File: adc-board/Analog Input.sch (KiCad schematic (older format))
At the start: 56 parts, among them J1 BHR-44-HUA, U1 Opamp_Quad_Generic, U2 Opamp_Quad_Generic, U29 AP7361C-33E-13, U3 Opamp_Quad_Generic, U4 Opamp_Quad_Generic, U5 Opamp_Quad_Generic, U6 Opamp_Quad_Generic

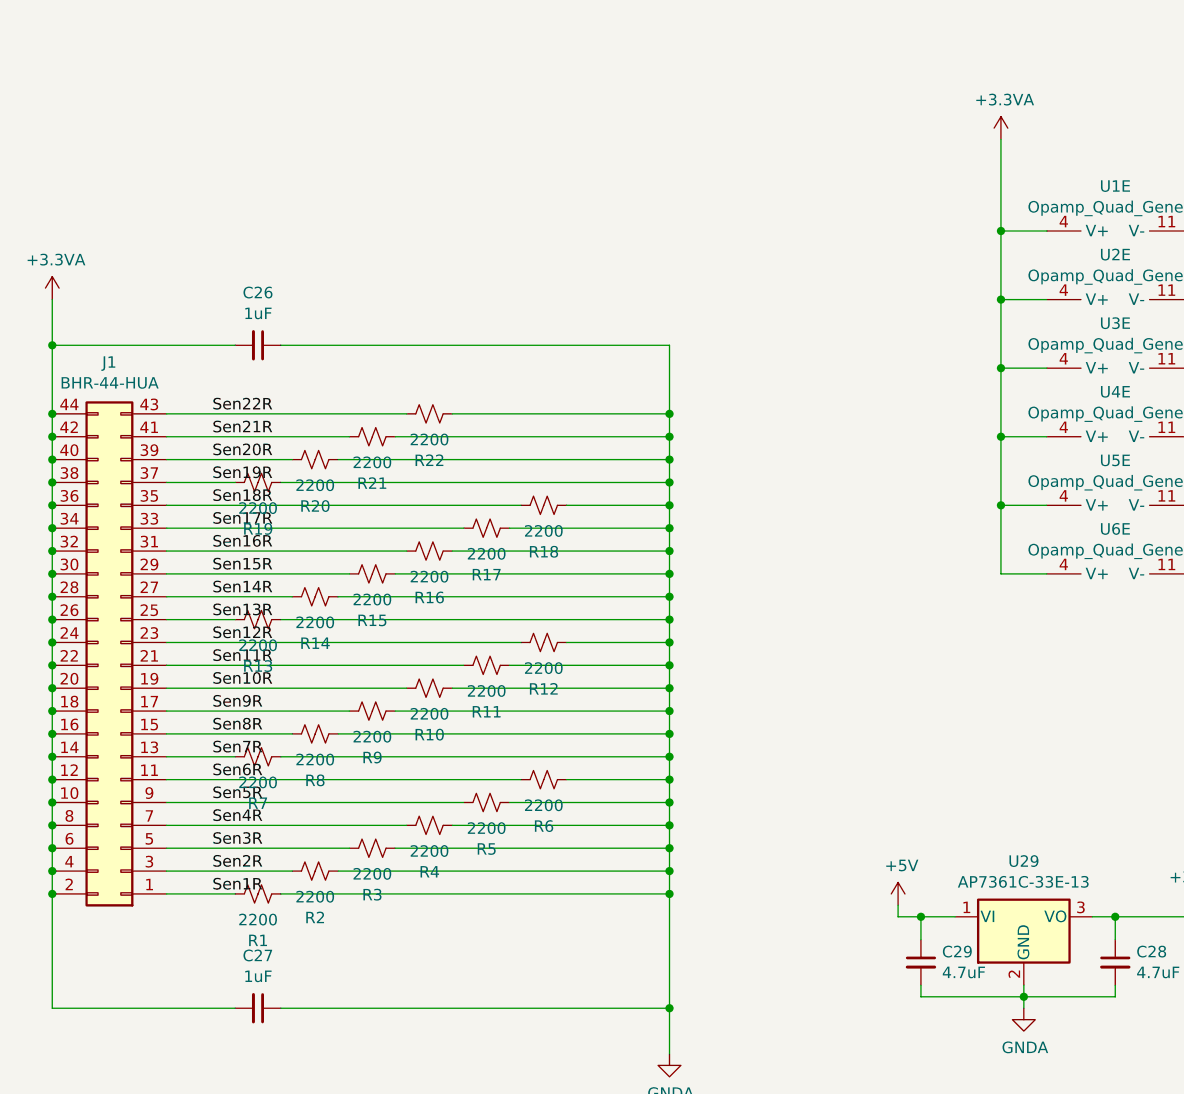
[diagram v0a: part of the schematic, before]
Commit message: correct RS485 termination resistors, adjust ground pours
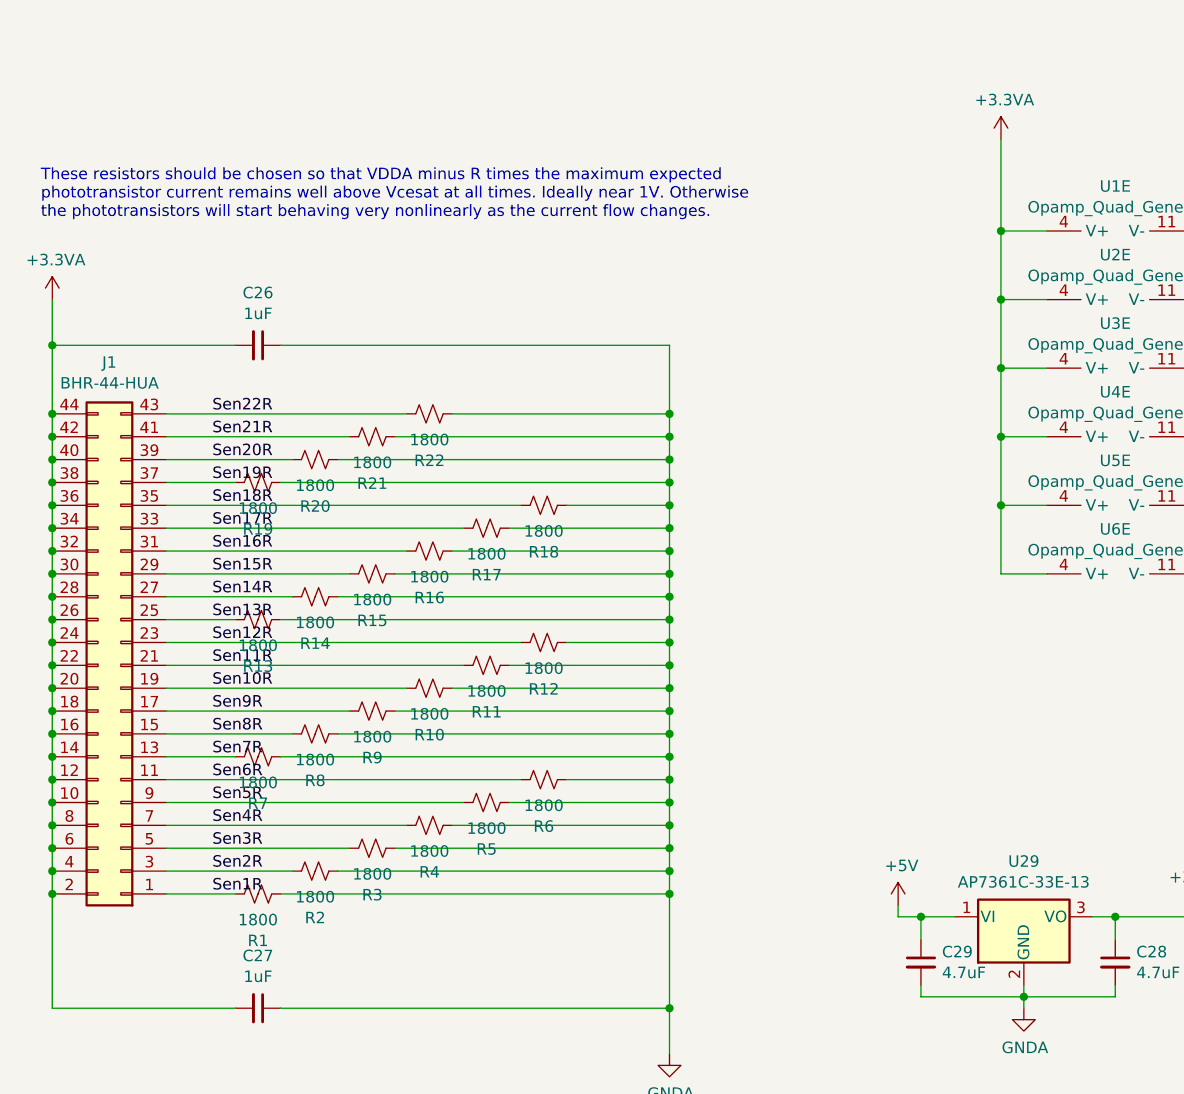
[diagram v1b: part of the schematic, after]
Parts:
- R1, R10, R11, R12, R13, R14, R15, R16, R17, R18, R19, R2, R20, R21, R22, R3, R4, R5, R6, R7, R8, R9: value 2200 -> 1800
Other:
- note added: "These resistors should be chosen so that VDDA minus R times the maximum expected\nphototransistor current remains well above Vcesat at all times. Ideally near 1V. Otherwise\nthe phototransistors will start behaving very nonlinearly as the current flow changes."
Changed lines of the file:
@@
 P 1850 6300
 F 0 "R2" V 1645 6300 50  0000 C CNN
-F 1 "2200" V 1736 6300 50  0000 C CNN
+F 1 "1800" V 1736 6300 50  0000 C CNN
 F 2 "Resistors_SMD:R_0805" H 1850 6300 50  0001 C CNN
 F 3 "~" H 1850 6300 50  0001 C CNN
@@
 P 2100 6200
 F 0 "R3" V 1895 6200 50  0000 C CNN
-F 1 "2200" V 1986 6200 50  0000 C CNN
+F 1 "1800" V 1986 6200 50  0000 C CNN
 F 2 "Resistors_SMD:R_0805" H 2100 6200 50  0001 C CNN
 F 3 "~" H 2100 6200 50  0001 C CNN
@@
 P 2350 6100
 F 0 "R4" V 2145 6100 50  0000 C CNN
-F 1 "2200" V 2236 6100 50  0000 C CNN
+F 1 "1800" V 2236 6100 50  0000 C CNN
 F 2 "Resistors_SMD:R_0805" H 2350 6100 50  0001 C CNN
 F 3 "~" H 2350 6100 50  0001 C CNN
@@
 P 2600 6000
 F 0 "R5" V 2395 6000 50  0000 C CNN
-F 1 "2200" V 2486 6000 50  0000 C CNN
+F 1 "1800" V 2486 6000 50  0000 C CNN
 F 2 "Resistors_SMD:R_0805" H 2600 6000 50  0001 C CNN
 F 3 "~" H 2600 6000 50  0001 C CNN
@@
 P 2850 5900
 F 0 "R6" V 2645 5900 50  0000 C CNN
-F 1 "2200" V 2736 5900 50  0000 C CNN
+F 1 "1800" V 2736 5900 50  0000 C CNN
 F 2 "Resistors_SMD:R_0805" H 2850 5900 50  0001 C CNN
 F 3 "~" H 2850 5900 50  0001 C CNN
@@
 P 1600 5800
 F 0 "R7" V 1395 5800 50  0000 C CNN
-F 1 "2200" V 1486 5800 50  0000 C CNN
+F 1 "1800" V 1486 5800 50  0000 C CNN
 F 2 "Resistors_SMD:R_0805" H 1600 5800 50  0001 C CNN
 F 3 "~" H 1600 5800 50  0001 C CNN
@@
 P 1850 5700
 F 0 "R8" V 1645 5700 50  0000 C CNN
-F 1 "2200" V 1736 5700 50  0000 C CNN
+F 1 "1800" V 1736 5700 50  0000 C CNN
 F 2 "Resistors_SMD:R_0805" H 1850 5700 50  0001 C CNN
 F 3 "~" H 1850 5700 50  0001 C CNN
@@
 P 2100 5600
 F 0 "R9" V 1895 5600 50  0000 C CNN
-F 1 "2200" V 1986 5600 50  0000 C CNN
+F 1 "1800" V 1986 5600 50  0000 C CNN
 F 2 "Resistors_SMD:R_0805" H 2100 5600 50  0001 C CNN
 F 3 "~" H 2100 5600 50  0001 C CNN
@@
 P 2350 5500
 F 0 "R10" V 2145 5500 50  0000 C CNN
-F 1 "2200" V 2236 5500 50  0000 C CNN
+F 1 "1800" V 2236 5500 50  0000 C CNN
 F 2 "Resistors_SMD:R_0805" H 2350 5500 50  0001 C CNN
 F 3 "~" H 2350 5500 50  0001 C CNN
@@
 P 2600 5400
 F 0 "R11" V 2395 5400 50  0000 C CNN
-F 1 "2200" V 2486 5400 50  0000 C CNN
+F 1 "1800" V 2486 5400 50  0000 C CNN
 F 2 "Resistors_SMD:R_0805" H 2600 5400 50  0001 C CNN
 F 3 "~" H 2600 5400 50  0001 C CNN
@@
 P 2850 5300
 F 0 "R12" V 2645 5300 50  0000 C CNN
-F 1 "2200" V 2736 5300 50  0000 C CNN
+F 1 "1800" V 2736 5300 50  0000 C CNN
 F 2 "Resistors_SMD:R_0805" H 2850 5300 50  0001 C CNN
 F 3 "~" H 2850 5300 50  0001 C CNN
@@
 P 1600 5200
 F 0 "R13" V 1395 5200 50  0000 C CNN
-F 1 "2200" V 1486 5200 50  0000 C CNN
+F 1 "1800" V 1486 5200 50  0000 C CNN
 F 2 "Resistors_SMD:R_0805" H 1600 5200 50  0001 C CNN
 F 3 "~" H 1600 5200 50  0001 C CNN
@@
 P 1850 5100
 F 0 "R14" V 1645 5100 50  0000 C CNN
-F 1 "2200" V 1736 5100 50  0000 C CNN
+F 1 "1800" V 1736 5100 50  0000 C CNN
 F 2 "Resistors_SMD:R_0805" H 1850 5100 50  0001 C CNN
 F 3 "~" H 1850 5100 50  0001 C CNN
@@
 P 2100 5000
 F 0 "R15" V 1895 5000 50  0000 C CNN
-F 1 "2200" V 1986 5000 50  0000 C CNN
+F 1 "1800" V 1986 5000 50  0000 C CNN
 F 2 "Resistors_SMD:R_0805" H 2100 5000 50  0001 C CNN
 F 3 "~" H 2100 5000 50  0001 C CNN
@@
 P 2350 4900
 F 0 "R16" V 2145 4900 50  0000 C CNN
-F 1 "2200" V 2236 4900 50  0000 C CNN
+F 1 "1800" V 2236 4900 50  0000 C CNN
 F 2 "Resistors_SMD:R_0805" H 2350 4900 50  0001 C CNN
 F 3 "~" H 2350 4900 50  0001 C CNN
@@
 P 2600 4800
 F 0 "R17" V 2395 4800 50  0000 C CNN
-F 1 "2200" V 2486 4800 50  0000 C CNN
+F 1 "1800" V 2486 4800 50  0000 C CNN
 F 2 "Resistors_SMD:R_0805" H 2600 4800 50  0001 C CNN
 F 3 "~" H 2600 4800 50  0001 C CNN
@@
 P 2850 4700
 F 0 "R18" V 2645 4700 50  0000 C CNN
-F 1 "2200" V 2736 4700 50  0000 C CNN
+F 1 "1800" V 2736 4700 50  0000 C CNN
 F 2 "Resistors_SMD:R_0805" H 2850 4700 50  0001 C CNN
 F 3 "~" H 2850 4700 50  0001 C CNN
@@
 P 1600 4600
 F 0 "R19" V 1395 4600 50  0000 C CNN
-F 1 "2200" V 1486 4600 50  0000 C CNN
+F 1 "1800" V 1486 4600 50  0000 C CNN
 F 2 "Resistors_SMD:R_0805" H 1600 4600 50  0001 C CNN
 F 3 "~" H 1600 4600 50  0001 C CNN
@@
 P 1850 4500
 F 0 "R20" V 1645 4500 50  0000 C CNN
-F 1 "2200" V 1736 4500 50  0000 C CNN
+F 1 "1800" V 1736 4500 50  0000 C CNN
 F 2 "Resistors_SMD:R_0805" H 1850 4500 50  0001 C CNN
 F 3 "~" H 1850 4500 50  0001 C CNN
@@
 P 2100 4400
 F 0 "R21" V 1895 4400 50  0000 C CNN
-F 1 "2200" V 1986 4400 50  0000 C CNN
+F 1 "1800" V 1986 4400 50  0000 C CNN
 F 2 "Resistors_SMD:R_0805" H 2100 4400 50  0001 C CNN
 F 3 "~" H 2100 4400 50  0001 C CNN
@@
 P 2350 4300
 F 0 "R22" V 2145 4300 50  0000 C CNN
-F 1 "2200" V 2236 4300 50  0000 C CNN
+F 1 "1800" V 2236 4300 50  0000 C CNN
 F 2 "Resistors_SMD:R_0805" H 2350 4300 50  0001 C CNN
 F 3 "~" H 2350 4300 50  0001 C CNN
@@
 P 1600 6400
 F 0 "R1" V 1395 6400 50  0000 C CNN
-F 1 "2200" V 1486 6400 50  0000 C CNN
+F 1 "1800" V 1486 6400 50  0000 C CNN
 F 2 "Resistors_SMD:R_0805" H 1600 6400 50  0001 C CNN
 F 3 "~" H 1600 6400 50  0001 C CNN
@@
 Wire Wire Line
 	5350 6500 5700 6500
+Text Notes 650  3450 0    50   ~ 0
+These resistors should be chosen so that VDDA minus R times the maximum expected\nphototransistor current remains well above Vcesat at all times. Ideally near 1V. Otherwise\nthe phototransistors will start behaving very nonlinearly as the current flow changes.
 $EndSCHEMATC

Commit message: alternative power inputs; cap on NRST; 3.3V reg thermal work on PCB
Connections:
- net +3.3VA: now also U6.10 (+), U6.12 (+)
- net GNDA: no longer U6.10 (+), U6.12 (+)
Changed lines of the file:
@@
 	12800 7800 12850 7800
 Wire Wire Line
-	10800 7800 10800 7600
-Wire Wire Line
 	10800 7600 10850 7600
-Wire Wire Line
-	12800 7800 12800 7600
 Wire Wire Line
 	12800 7600 12850 7600
@@
 Wire Wire Line
 	12800 7800 12800 7900
-Connection ~ 12800 7800
 Wire Wire Line
 	10800 7800 10800 7900
-Connection ~ 10800 7800
 $Comp
 L Device:Opamp_Quad_Generic U1
@@
 Text Notes 650  3450 0    50   ~ 0
 These resistors should be chosen so that VDDA minus R times the maximum expected\nphototransistor current remains well above Vcesat at all times. Ideally near 1V. Otherwise\nthe phototransistors will start behaving very nonlinearly as the current flow changes.
+$Comp
+L power:+3.3VA #PWR0137
+U 1 1 5FB624A5
+P 10800 7550
+F 0 "#PWR0137" H 10800 7400 50  0001 C CNN
+F 1 "+3.3VA" H 10815 7723 50  0000 C CNN
+F 2 "" H 10800 7550 50  0001 C CNN
+F 3 "" H 10800 7550 50  0001 C CNN
+	1    10800 7550
+	1    0    0    -1
+$EndComp
+$Comp
+L power:+3.3VA #PWR0140
+U 1 1 5FB64A1B
+P 12800 7550
+F 0 "#PWR0140" H 12800 7400 50  0001 C CNN
+F 1 "+3.3VA" H 12815 7723 50  0000 C CNN
+F 2 "" H 12800 7550 50  0001 C CNN
+F 3 "" H 12800 7550 50  0001 C CNN
+	1    12800 7550
+	1    0    0    -1
+$EndComp
+Wire Wire Line
+	12800 7600 12800 7550
+Wire Wire Line
+	10800 7600 10800 7550
 $EndSCHEMATC

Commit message: move USB ferrite closer to connector; add VCC pad near BOOT pulldown
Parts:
- U29: value AP7361C-33E-13 -> AP2114HA-3.3TRG1
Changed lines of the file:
@@
 AR Path="/5FA7E425/60593179" Ref="U29"  Part="1"
 F 0 "U29" H 4950 6742 50  0000 C CNN
-F 1 "AP7361C-33E-13" H 4950 6651 50  0000 C CNN
+F 1 "AP2114HA-3.3TRG1" H 4950 6651 50  0000 C CNN
 F 2 "TO_SOT_Packages_SMD:SOT-223-3_TabPin2" H 4950 6725 50  0001 C CIN
 F 3 "https://www.diodes.com/assets/Datasheets/AP7361C.pdf" H 4950 6450 50  0001 C CNN

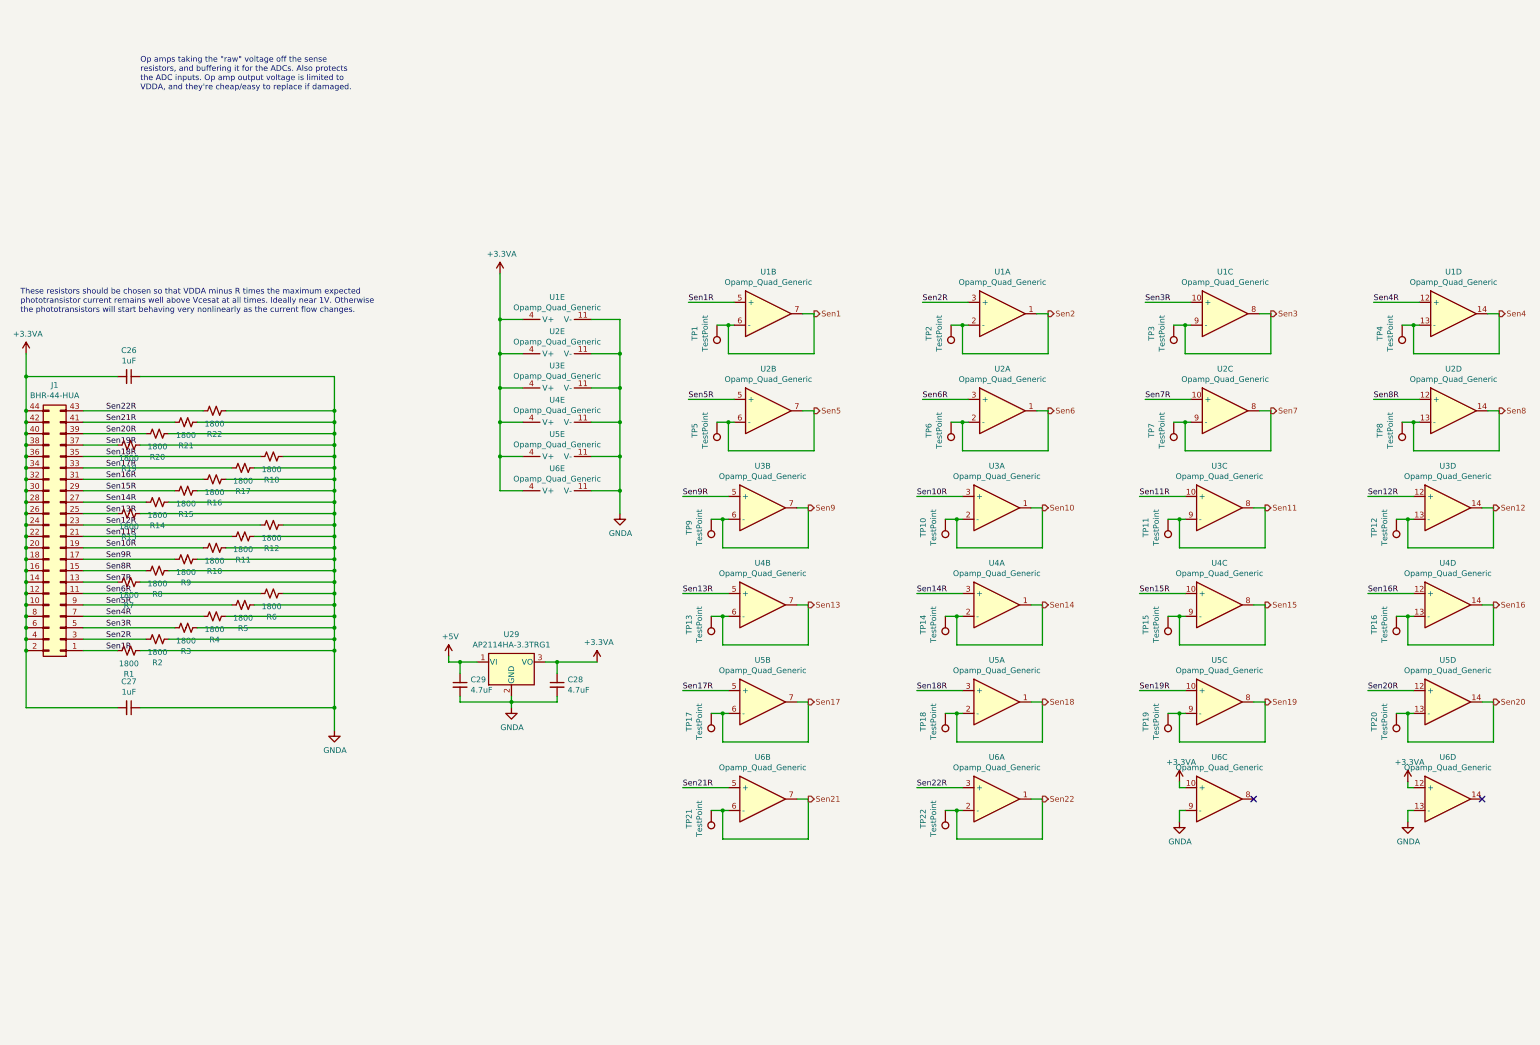
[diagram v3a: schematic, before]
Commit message: Convert analog sensing over to transimpedance amplifiers
Also switched opamps for the TSSOP14 package, and replaced the
fancy voltage reference with a simple 2.0V regulator.
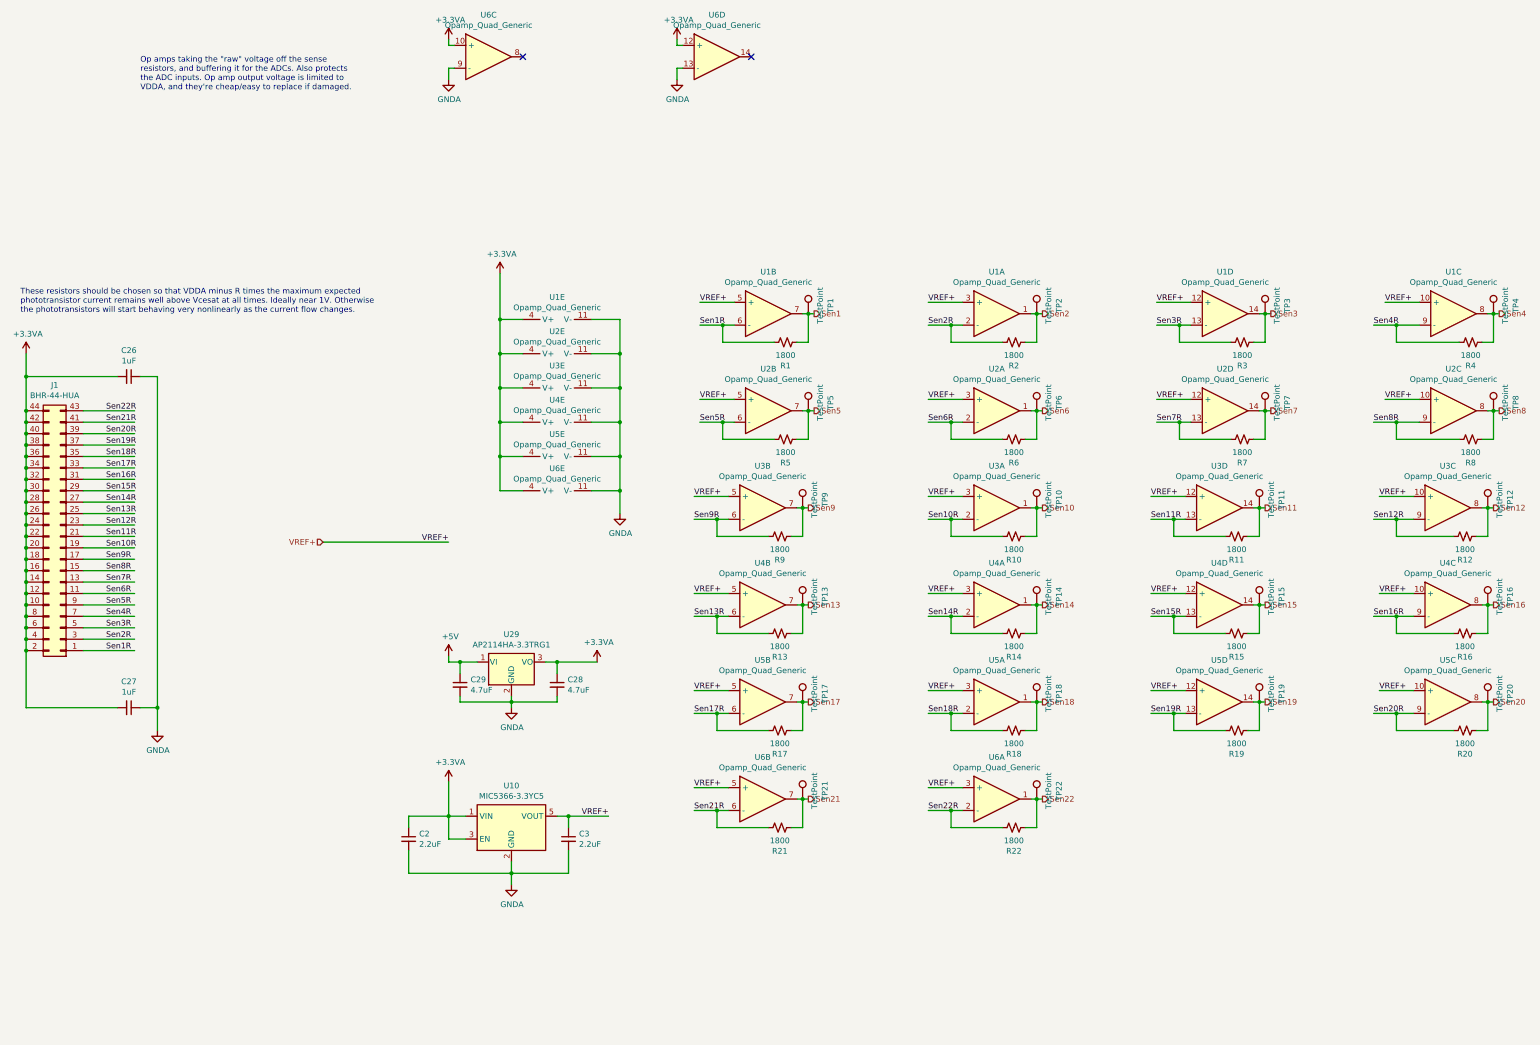
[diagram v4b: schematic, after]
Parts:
- added C2, C3: 2.2uF, Capacitors_SMD:C_0805, symbol Device:C_Small
- added U10: MIC5366-3.3YC5, TO_SOT_Packages_SMD:SOT-353_SC-70-5_Handsoldering, symbol Regulator_Linear:MIC5366-3.3YC5
- U1, U2, U3, U4, U5, U6: footprint SMD_Packages:SOIC-14_N -> Housings_SSOP:TSSOP-14_4.4x5mm_Pitch0.65mm
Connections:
- net labels added: VREF+
- wire segments 295 -> 311
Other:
- moved on the sheet: R1, R10, R11, R12, R13, R14, R15, R16, R17, R18, R19, R2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

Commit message: Repair some copper pour damage I did, and update notes in the schematic.
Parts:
- U10: value MIC5366-3.3YC5 -> MIC5366-2.0YC5
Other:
- note added: "The resistors here set the gain of the transimpedance amplifiers.\nThey should be (max expected current) * R =~ VREF+"
- note removed: "Op amps taking the "raw" voltage off the sense\nresistors, and buffering it for the ADCs. Also protects\nthe ADC inputs. Op amp output voltage is limited to\nVDDA, and they're cheap/easy to replace if damaged."
- note removed: "These resistors should be chosen so that VDDA minus R times the maximum expected\nphototransistor current remains well above Vcesat at all times. Ideally near 1V. Otherwise\nthe phototransistors will start behaving very nonlinearly as the current flow changes."
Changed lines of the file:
@@
 	1    0    0    -1
 $EndComp
-Text Notes 1700 1500 0    50   ~ 0
-Op amps taking the "raw" voltage off the sense\nresistors, and buffering it for the ADCs. Also protects\nthe ADC inputs. Op amp output voltage is limited to\nVDDA, and they're cheap/easy to replace if damaged.
 $Comp
 L power:+3.3VA #PWR0123
@@
 Wire Wire Line
 	5350 6500 5700 6500
-Text Notes 650  3450 0    50   ~ 0
-These resistors should be chosen so that VDDA minus R times the maximum expected\nphototransistor current remains well above Vcesat at all times. Ideally near 1V. Otherwise\nthe phototransistors will start behaving very nonlinearly as the current flow changes.
+Text Notes 7850 2750 0    50   ~ 0
+The resistors here set the gain of the transimpedance amplifiers.\nThey should be (max expected current) * R =~ VREF+
 $Comp
 L power:+3.3VA #PWR0137
@@
 AR Path="/5FA7E425/61D87A67" Ref="U10"  Part="1"
 F 0 "U10" H 4950 8317 50  0000 C CNN
-F 1 "MIC5366-3.3YC5" H 4950 8226 50  0000 C CNN
+F 1 "MIC5366-2.0YC5" H 4950 8226 50  0000 C CNN
 F 2 "TO_SOT_Packages_SMD:SOT-353_SC-70-5_Handsoldering" H 4950 8300 50  0001 C CNN
 F 3 "http://ww1.microchip.com/downloads/en/DeviceDoc/mic5365.pdf" H 4650 8750 50  0001 C CNN
